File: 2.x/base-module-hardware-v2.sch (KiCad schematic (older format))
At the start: 2 parts, among them P1 CONN_5X2, P2 CONN_5X2

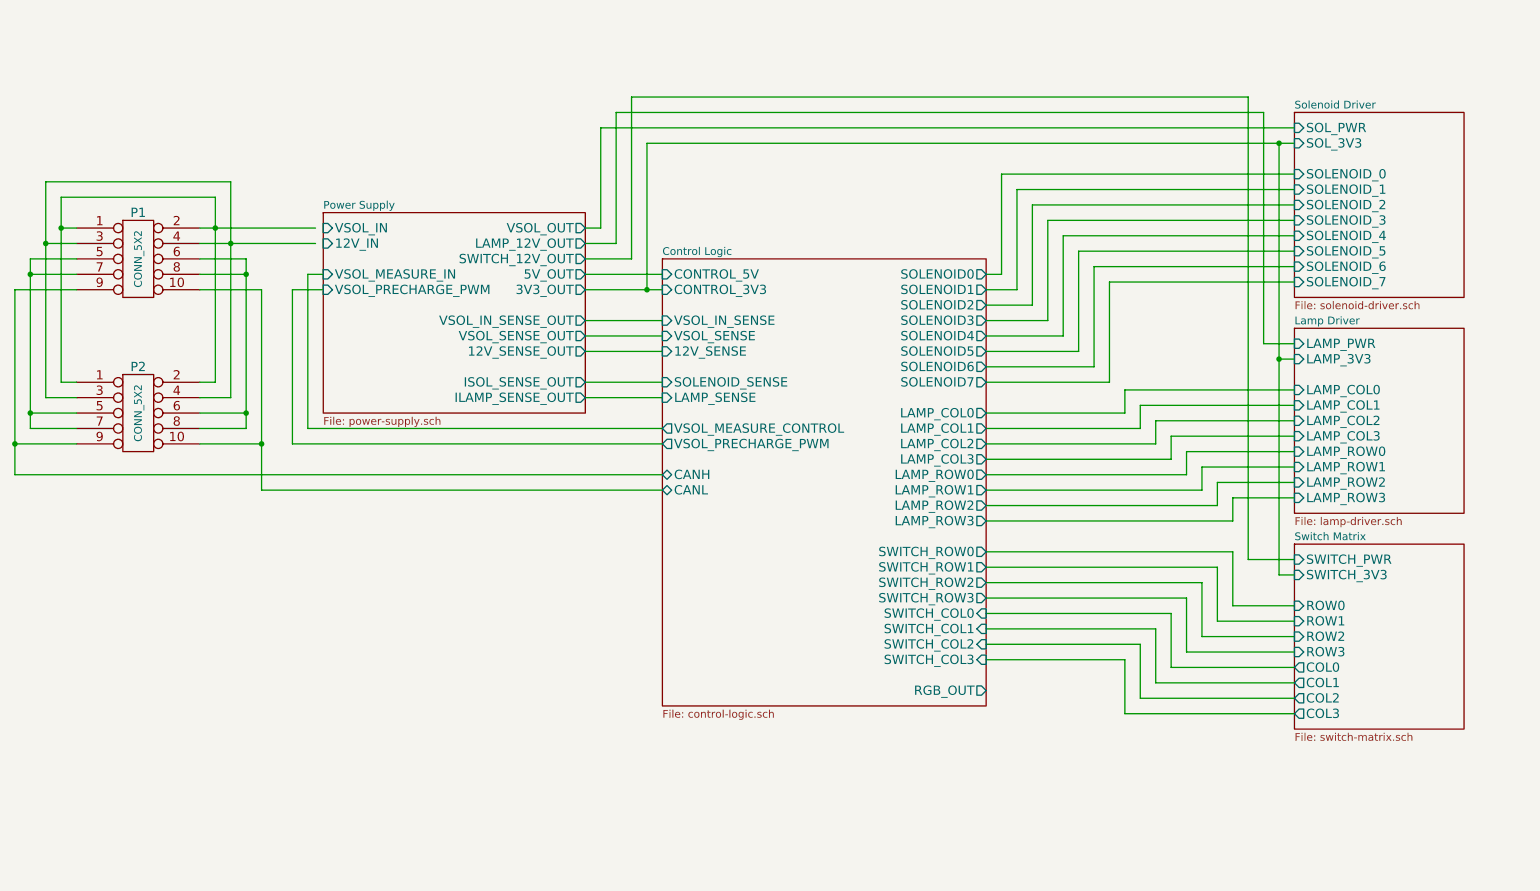
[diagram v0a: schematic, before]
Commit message: Added RGB output and finished power supply monitor schematic, including new current monitor and voltage monitor divider values.
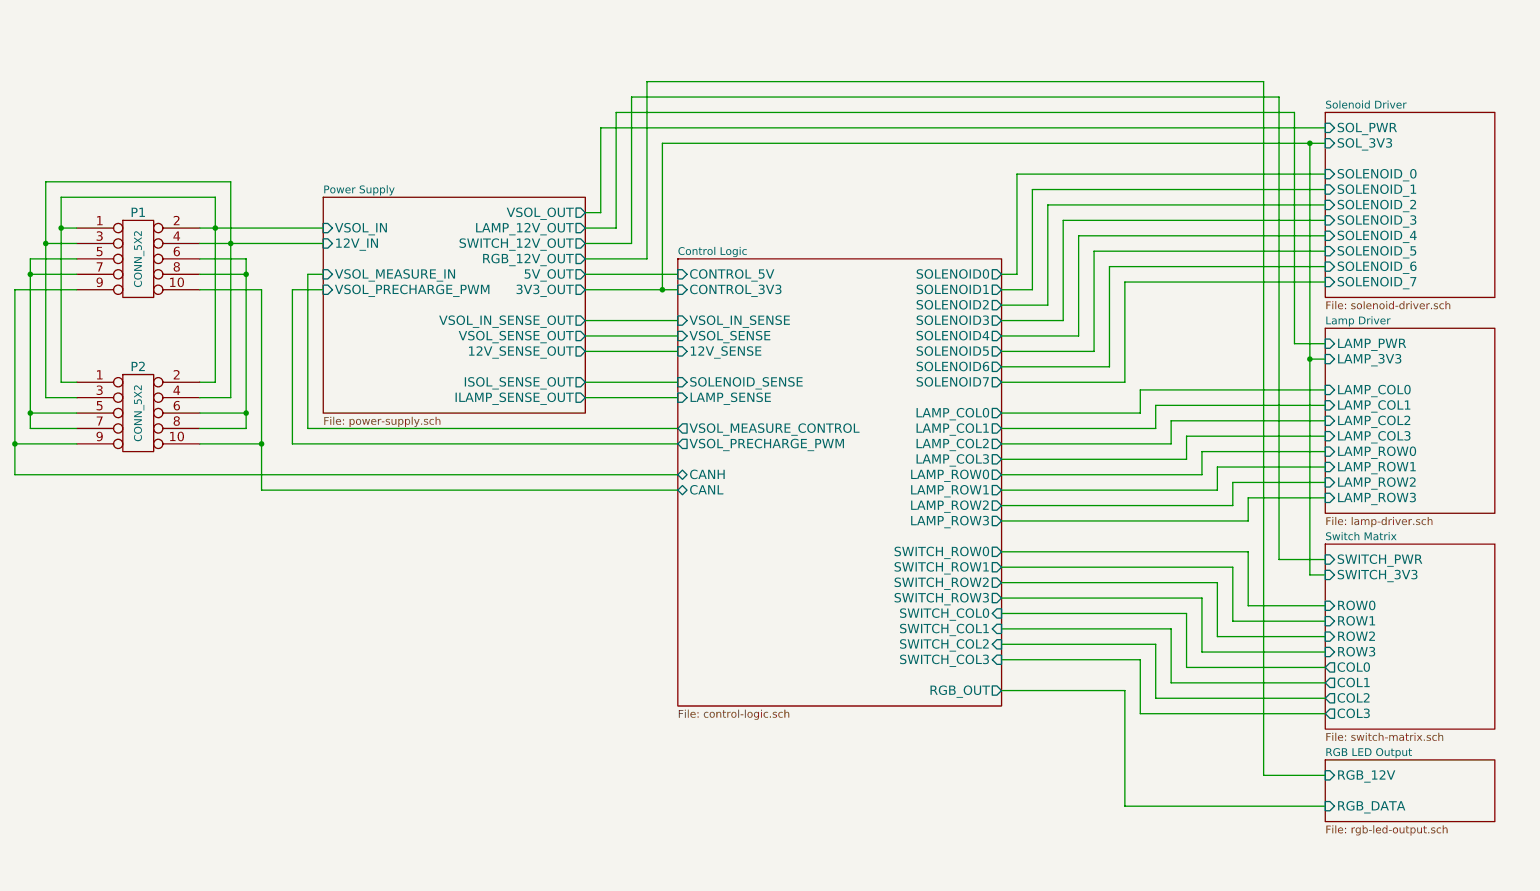
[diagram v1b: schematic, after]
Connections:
- net Power Supply/12V_IN: now also P1.3, P1.4, P2.3, P2.4
- net Power Supply/VSOL_IN: now also P1.1, P1.2, P2.1, P2.2

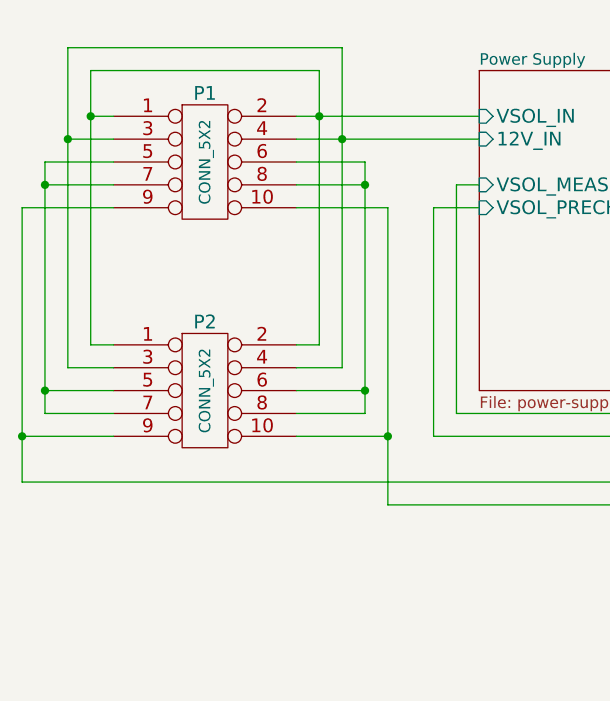
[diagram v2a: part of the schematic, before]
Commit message: Cleaning up schematic Updating solenoid driver to use 12V for MOSFET gates instead of Vsol so we never exceed Vgs_max
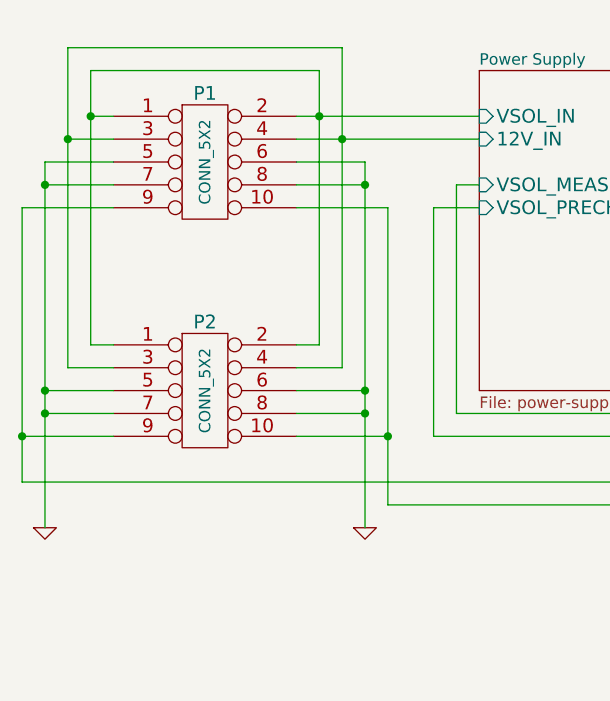
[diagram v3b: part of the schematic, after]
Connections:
- net GND: now reaches P1.5, P1.7, P2.5, P2.7
- net GND: now also P1.6, P1.8, P2.6, P2.8
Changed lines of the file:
@@
 LIBS:nxp_armmcu
 LIBS:base-module-hardware-v2-cache
-EELAYER 27 0
+EELAYER 25 0
 EELAYER END
 $Descr USLetter 11000 8500
@@
 	1050 2400 750  2400
 Wire Wire Line
-	750  2400 750  3500
+	750  2400 750  4000
 Wire Wire Line
 	750  3500 1050 3500
@@
 	1850 2400 2150 2400
 Wire Wire Line
-	2150 2400 2150 3500
+	2150 2400 2150 4000
 Wire Wire Line
 	2150 3500 1850 3500
@@
 Wire Wire Line
 	8750 5750 9150 5750
+$Comp
+L GND #PWR?
+U 1 1 538113F2
+P 750 4000
+F 0 "#PWR?" H 750 4000 30  0001 C CNN
+F 1 "GND" H 750 3930 30  0001 C CNN
+F 2 "" H 750 4000 60  0000 C CNN
+F 3 "" H 750 4000 60  0000 C CNN
+	1    750  4000
+	1    0    0    -1
+$EndComp
+$Comp
+L GND #PWR?
+U 1 1 53811406
+P 2150 4000
+F 0 "#PWR?" H 2150 4000 30  0001 C CNN
+F 1 "GND" H 2150 3930 30  0001 C CNN
+F 2 "" H 2150 4000 60  0000 C CNN
+F 3 "" H 2150 4000 60  0000 C CNN
+	1    2150 4000
+	1    0    0    -1
+$EndComp
+Connection ~ 2150 3500
+Connection ~ 750  3500
 $EndSCHEMATC

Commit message: Started layout on 2.0
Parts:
- removed P1, P2: CONN_5X2, symbol CONN_5X2
- added P1, P2: PINBALL-CONNECTOR, PinballParts:PINBALL-CONNECTOR-V, symbol PINBALL-CONNECTOR
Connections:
- net Control Logic/CANH: now also P1.5 (CANH), P2.5 (CANH)
- net Control Logic/CANL: now also P1.10 (CANL), P2.10 (CANL)
- net GND: now also P1.3 (GND), P1.4 (GND), P1.8 (GND), P1.9 (GND), P2.3 (GND), P2.4 (GND), P2.8 (GND), P2.9 (GND)
- net Power Supply/12V_IN: now also P1.2 (12V), P1.7 (12V), P2.2 (12V), P2.7 (12V)
- net Power Supply/VSOL_IN: now also P1.1 (VSOL), P1.6 (VSOL), P2.1 (VSOL), P2.6 (VSOL)
